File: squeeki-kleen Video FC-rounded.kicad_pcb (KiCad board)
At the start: 2 copper layers, 50.8 x 17.8 mm, 49 parts, among them J1 VCC, J2 VOUT, J3 GND, J4 Conn_Coaxial, Q1 MMBT3906

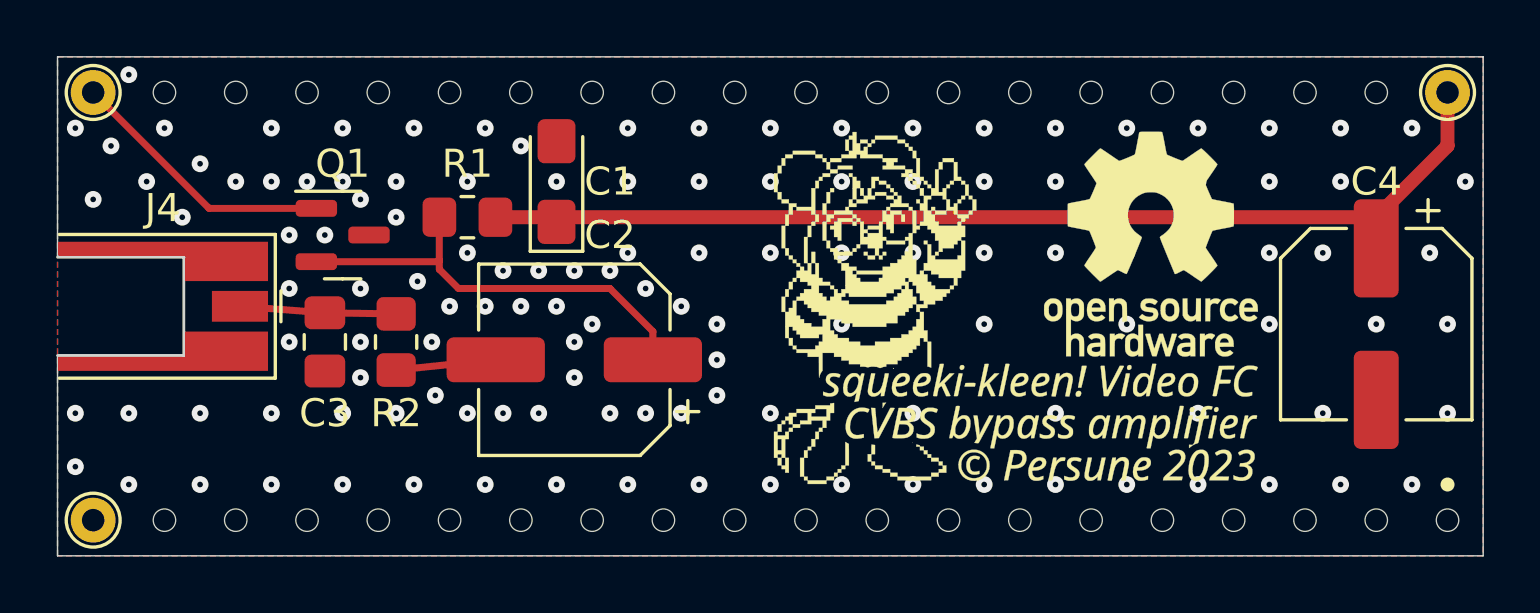
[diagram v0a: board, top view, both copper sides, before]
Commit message: Big changes
- Fix MMBT3906 pinout
- Use NPTH instead of edge cut circles
- Update silkscreen art
- Add 100uF electrolytic capacitor for power
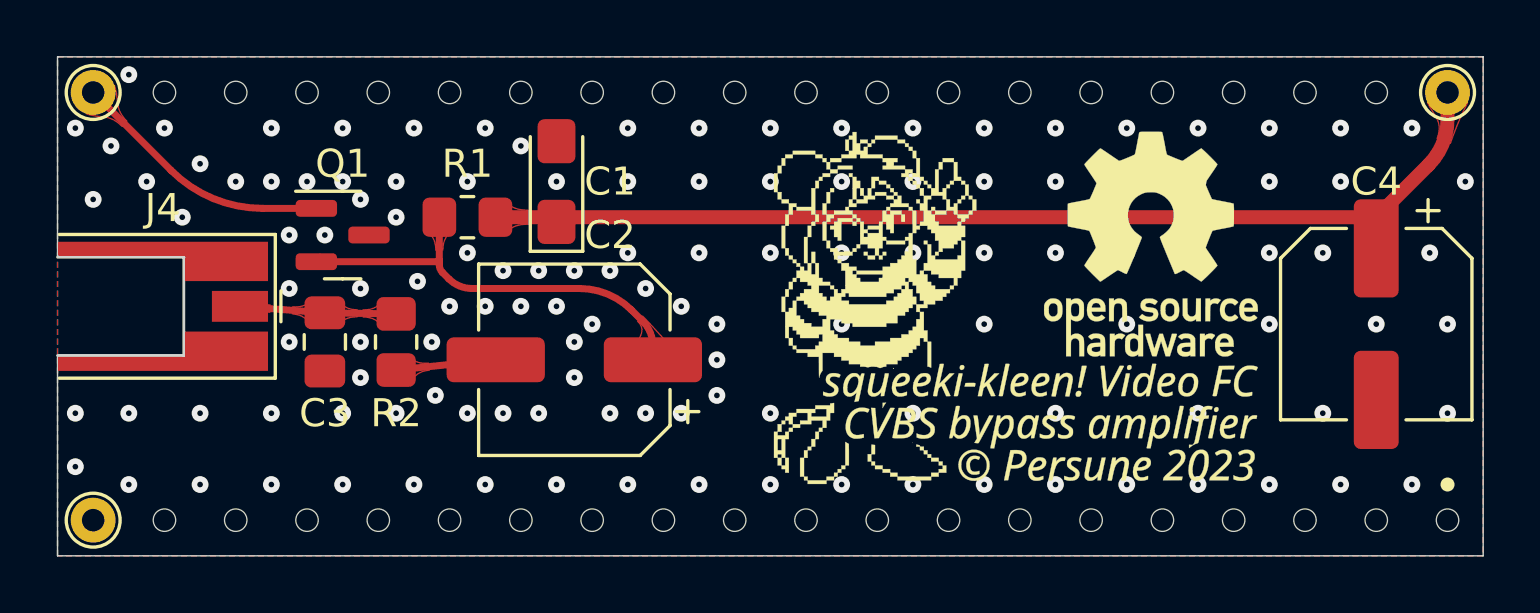
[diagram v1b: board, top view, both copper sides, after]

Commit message: Update silkscreen art to add QR code
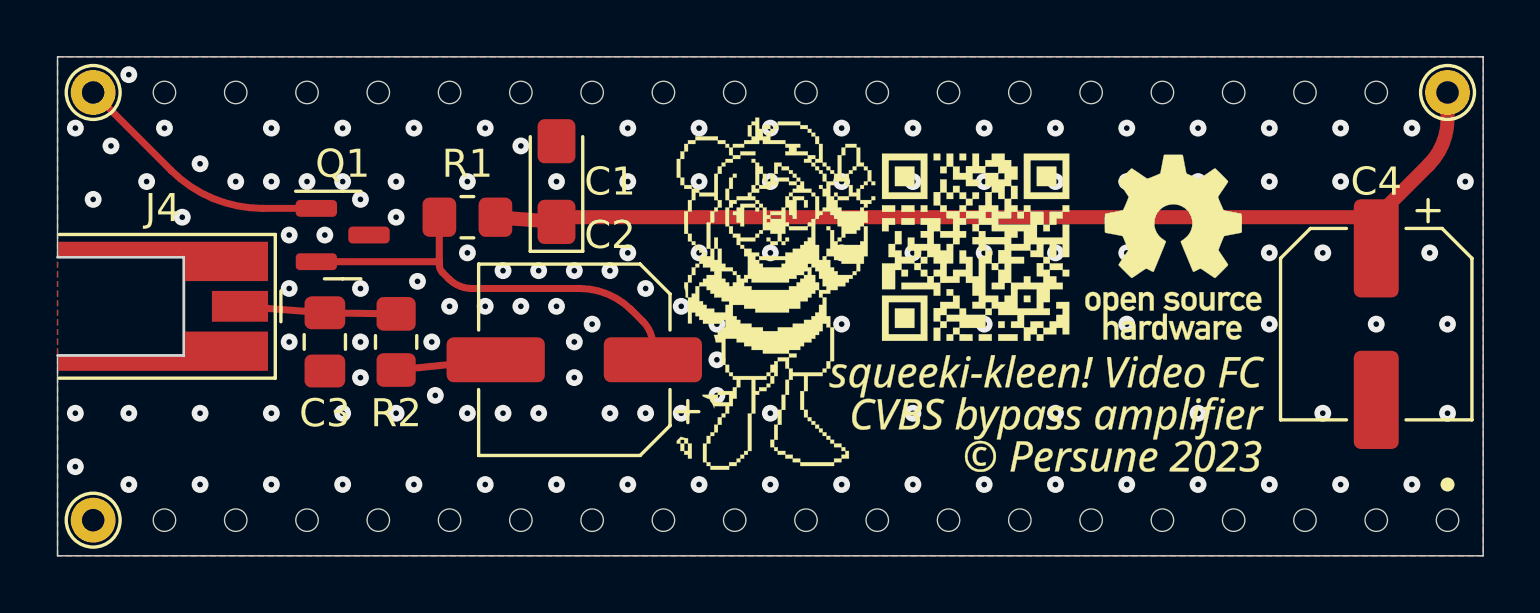
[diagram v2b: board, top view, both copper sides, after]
